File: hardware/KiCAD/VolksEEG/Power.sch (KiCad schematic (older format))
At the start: 27 parts, among them U3 LP3990MF-3.3, U4 LM2660MX, U5 TPS78425Q, U6 TPS72325Q

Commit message: Added Digi-key's kicad component libraries, some work done on power, think this will change but capturing it here for posterity.
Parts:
- removed C? (x2): 2.2u, Capacitor_SMD:C_0603_1608Metric_Pad1.08x0.95mm_HandSolder, symbol Device:C
- removed C?: 10u, Capacitor_SMD:C_0603_1608Metric_Pad1.08x0.95mm_HandSolder, symbol Device:C
- removed L?: 3.3u, symbol Device:L
- removed U3: LP3990MF-3.3, VolksEEG:SOT95P280X145-5N, symbol VolksEEG:LP3990MF-3.3
- added C? (x5): 100n, symbol Device:C
- added C? (x4): 1u, symbol Device:C
- added C?: 10u, Capacitor_SMD:C_0603_1608Metric_Pad1.08x0.95mm_HandSolder, symbol Device:C
- added C? (x2): 2.2u, Capacitor_SMD:C_0603_1608Metric_Pad1.08x0.95mm_HandSolder, symbol Device:C
- added C?: 10n, Capacitor_SMD:C_0603_1608Metric_Pad1.08x0.95mm_HandSolder, symbol Device:C
- added L?: 3.3u, symbol Device:L
- added U?: LP3990MF-3.3, VolksEEG:SOT95P280X145-5N, symbol VolksEEG:LP3990MF-3.3
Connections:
- net labels added: +2V5_ads, +3V3_ads, +5V_iso, -2V5_ads, GND2, VDD
- net labels removed: +3V3, GNDD, VDC
- wire segments 75 -> 130
- no-connect marks 5 -> 4
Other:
- note added: "3.3V Digital Voltage Supply"
- note removed: "3.3V Voltage Supply"
- moved on the sheet: C2, C4, C7, C8, C9, C?, L?, R?, U4, U5, U6

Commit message: Rejigged the power around so that the 3v3 supply is only generated once.
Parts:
- removed R?: 0, symbol Device:R
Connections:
- net labels added: +2V5_out, +3V3_out, -2V5_out
- net labels removed: +2V5_ads, +3V3_ads, -2V5_ads, GND2
- wire segments 130 -> 129
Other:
- moved on the sheet: C?
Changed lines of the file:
@@
 	2700 5300 3350 5300
 Wire Wire Line
-	2000 5300 1350 5300
+	2000 5300 1800 5300
 Wire Wire Line
 	1350 5300 1350 5150
@@
 Wire Wire Line
 	2000 4050 2000 3950
-Wire Wire Line
-	2000 5550 2000 5300
-Connection ~ 2000 5300
 Wire Wire Line
 	2000 5800 2000 5700
@@
 L power:GNDA #PWR?
 U 1 1 61837039
-P 4900 2300
-F 0 "#PWR?" H 4900 2050 50  0001 C CNN
-F 1 "GNDA" H 4905 2127 50  0000 C CNN
-F 2 "" H 4900 2300 50  0001 C CNN
-F 3 "" H 4900 2300 50  0001 C CNN
-	1    4900 2300
-	1    0    0    -1
-$EndComp
-$Comp
-L Device:R R?
-U 1 1 61837EDF
-P 3200 2200
-F 0 "R?" V 2993 2200 50  0000 C CNN
-F 1 "0" V 3084 2200 50  0000 C CNN
-F 2 "" V 3130 2200 50  0001 C CNN
-F 3 "~" H 3200 2200 50  0001 C CNN
-	1    3200 2200
-	0    1    1    0
+P 4900 1950
+F 0 "#PWR?" H 4900 1700 50  0001 C CNN
+F 1 "GNDA" H 4905 1777 50  0000 C CNN
+F 2 "" H 4900 1950 50  0001 C CNN
+F 3 "" H 4900 1950 50  0001 C CNN
+	1    4900 1950
+	1    0    0    -1
 $EndComp
 $Comp
@@
 L Device:C C?
 U 1 1 6195A2BF
-P 1500 1550
+P 1850 1550
 AR Path="/615BA255/6195A2BF" Ref="C?"  Part="1"
 AR Path="/61731DC5/6195A2BF" Ref="C?"  Part="1"
-F 0 "C?" H 1615 1596 50  0000 L CNN
-F 1 "2.2u" H 1615 1505 50  0000 L CNN
-F 2 "Capacitor_SMD:C_0603_1608Metric_Pad1.08x0.95mm_HandSolder" H 1538 1400 50  0001 C CNN
-F 3 "~" H 1500 1550 50  0001 C CNN
-	1    1500 1550
-	1    0    0    -1
-$EndComp
-Wire Wire Line
-	1500 1800 1500 1700
+F 0 "C?" H 1965 1596 50  0000 L CNN
+F 1 "2.2u" H 1965 1505 50  0000 L CNN
+F 2 "Capacitor_SMD:C_0603_1608Metric_Pad1.08x0.95mm_HandSolder" H 1888 1400 50  0001 C CNN
+F 3 "~" H 1850 1550 50  0001 C CNN
+	1    1850 1550
+	1    0    0    -1
+$EndComp
 Wire Wire Line
 	3800 1400 3800 1300
@@
 	1    0    0    -1
 $EndComp
-$Comp
-L power:GND2 #PWR?
-U 1 1 6195A2DE
-P 1500 1800
-AR Path="/61731DC5/6195A2DE" Ref="#PWR?"  Part="1"
-AR Path="/615BA255/6195A2DE" Ref="#PWR?"  Part="1"
-F 0 "#PWR?" H 1500 1550 50  0001 C CNN
-F 1 "GND2" H 1505 1627 50  0000 C CNN
-F 2 "" H 1500 1800 50  0001 C CNN
-F 3 "" H 1500 1800 50  0001 C CNN
-	1    1500 1800
-	1    0    0    -1
-$EndComp
-$Comp
-L power:GND2 #PWR?
-U 1 1 6195A2E4
-P 2450 2300
-AR Path="/61731DC5/6195A2E4" Ref="#PWR?"  Part="1"
-AR Path="/615BA255/6195A2E4" Ref="#PWR?"  Part="1"
-F 0 "#PWR?" H 2450 2050 50  0001 C CNN
-F 1 "GND2" H 2455 2127 50  0000 C CNN
-F 2 "" H 2450 2300 50  0001 C CNN
-F 3 "" H 2450 2300 50  0001 C CNN
-	1    2450 2300
-	1    0    0    -1
-$EndComp
-Wire Wire Line
-	1500 1400 1500 1300
-Connection ~ 1500 1300
-Wire Wire Line
-	2200 1550 2450 1550
-Text HLabel 1150 1300 0    50   Output ~ 0
+Wire Wire Line
+	1850 1400 1850 1300
+Text HLabel 1500 1300 0    50   Input ~ 0
 +5V_iso
 Wire Wire Line
-	1150 1300 1500 1300
+	1500 1300 1850 1300
 Wire Wire Line
 	4900 1150 4900 1300
@@
 	1    0    0    -1
 $EndComp
-Text HLabel 5100 1300 2    50   Input ~ 0
-+3V3_ads
+Text HLabel 5100 1300 2    50   Output ~ 0
++3V3_out
 Wire Wire Line
 	5100 1300 4900 1300
@@
 	1    0    0    -1
 $EndComp
-Wire Wire Line
-	2450 1700 2450 2200
-Connection ~ 2450 2200
-Wire Wire Line
-	2450 2200 2450 2300
 $Comp
 L power:GNDA #PWR?
 U 1 1 61970A4A
-P 3800 2300
-F 0 "#PWR?" H 3800 2050 50  0001 C CNN
-F 1 "GNDA" H 3805 2127 50  0000 C CNN
-F 2 "" H 3800 2300 50  0001 C CNN
-F 3 "" H 3800 2300 50  0001 C CNN
-	1    3800 2300
-	1    0    0    -1
-$EndComp
-Wire Wire Line
-	4900 1700 4900 2300
-Wire Wire Line
-	2450 2200 3050 2200
-Wire Wire Line
-	3800 1700 3800 2200
-Wire Wire Line
-	3350 2200 3800 2200
-Connection ~ 3800 2200
-Wire Wire Line
-	3800 2200 3800 2300
-Wire Wire Line
-	1500 1300 2200 1300
-Wire Wire Line
-	2200 1550 2200 1300
-Connection ~ 2200 1300
-Wire Wire Line
-	2200 1300 2450 1300
+P 3800 1950
+F 0 "#PWR?" H 3800 1700 50  0001 C CNN
+F 1 "GNDA" H 3805 1777 50  0000 C CNN
+F 2 "" H 3800 1950 50  0001 C CNN
+F 3 "" H 3800 1950 50  0001 C CNN
+	1    3800 1950
+	1    0    0    -1
+$EndComp
 Wire Wire Line
 	2000 3800 1850 3800
@@
 	1850 3550 2000 3550
 Text HLabel 5600 3550 2    50   Output ~ 0
-+2V5_ads
++2V5_out
 Text HLabel 5550 5300 2    50   Output ~ 0
--2V5_ads
+-2V5_out
 $Comp
 L Device:C C?
@@
 Wire Wire Line
 	5300 5300 5550 5300
+Wire Wire Line
+	2450 1550 2300 1550
+Wire Wire Line
+	2300 1550 2300 1300
+Wire Wire Line
+	2300 1300 2450 1300
+Wire Wire Line
+	1850 1300 2300 1300
+Connection ~ 1850 1300
+Connection ~ 2300 1300
+$Comp
+L power:GNDA #PWR?
+U 1 1 61A49E67
+P 2300 1950
+F 0 "#PWR?" H 2300 1700 50  0001 C CNN
+F 1 "GNDA" H 2305 1777 50  0000 C CNN
+F 2 "" H 2300 1950 50  0001 C CNN
+F 3 "" H 2300 1950 50  0001 C CNN
+	1    2300 1950
+	1    0    0    -1
+$EndComp
+$Comp
+L power:GNDA #PWR?
+U 1 1 61A4A061
+P 1850 1950
+F 0 "#PWR?" H 1850 1700 50  0001 C CNN
+F 1 "GNDA" H 1855 1777 50  0000 C CNN
+F 2 "" H 1850 1950 50  0001 C CNN
+F 3 "" H 1850 1950 50  0001 C CNN
+	1    1850 1950
+	1    0    0    -1
+$EndComp
+Wire Wire Line
+	1850 1700 1850 1950
+Wire Wire Line
+	2300 1950 2300 1700
+Wire Wire Line
+	2300 1700 2450 1700
+Wire Wire Line
+	3800 1950 3800 1700
+Wire Wire Line
+	4900 1700 4900 1950
+Wire Wire Line
+	2000 5550 1800 5550
+Wire Wire Line
+	1800 5550 1800 5300
+Connection ~ 1800 5300
+Wire Wire Line
+	1800 5300 1350 5300
 $EndSCHEMATC

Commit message: Updated names of heirarchical pins, finished referential montage configuration, added filter cap to ADS_nRST line, started putting ADS1299 gpios to a header.
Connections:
- net labels added: +2V5, +3V3, +5V, -2V5
- net labels removed: +2V5_out, +3V3_out, +5V_iso, -2V5_out
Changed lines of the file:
@@
 	1850 1400 1850 1300
 Text HLabel 1500 1300 0    50   Input ~ 0
-+5V_iso
++5V
 Wire Wire Line
 	1500 1300 1850 1300
@@
 $EndComp
 Text HLabel 5100 1300 2    50   Output ~ 0
-+3V3_out
++3V3
 Wire Wire Line
 	5100 1300 4900 1300
@@
 	1850 3550 2000 3550
 Text HLabel 5600 3550 2    50   Output ~ 0
-+2V5_out
++2V5
 Text HLabel 5550 5300 2    50   Output ~ 0
--2V5_out
+-2V5
 $Comp
 L Device:C C?

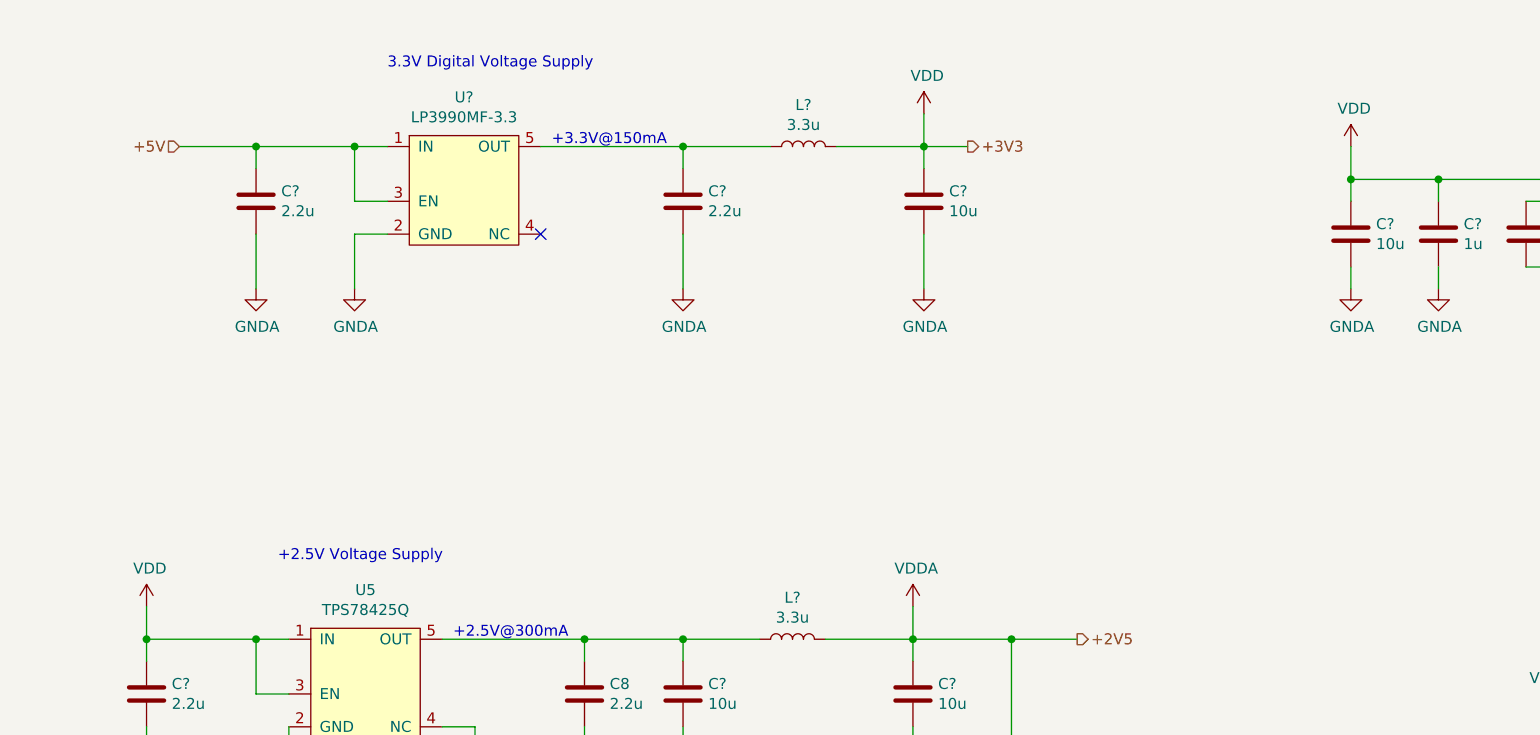
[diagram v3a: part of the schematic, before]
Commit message: Added custom power symbols for non isolated power. Seperated Analogue and digital supplies. finished putting the ADS1299 GPIOs to a header.
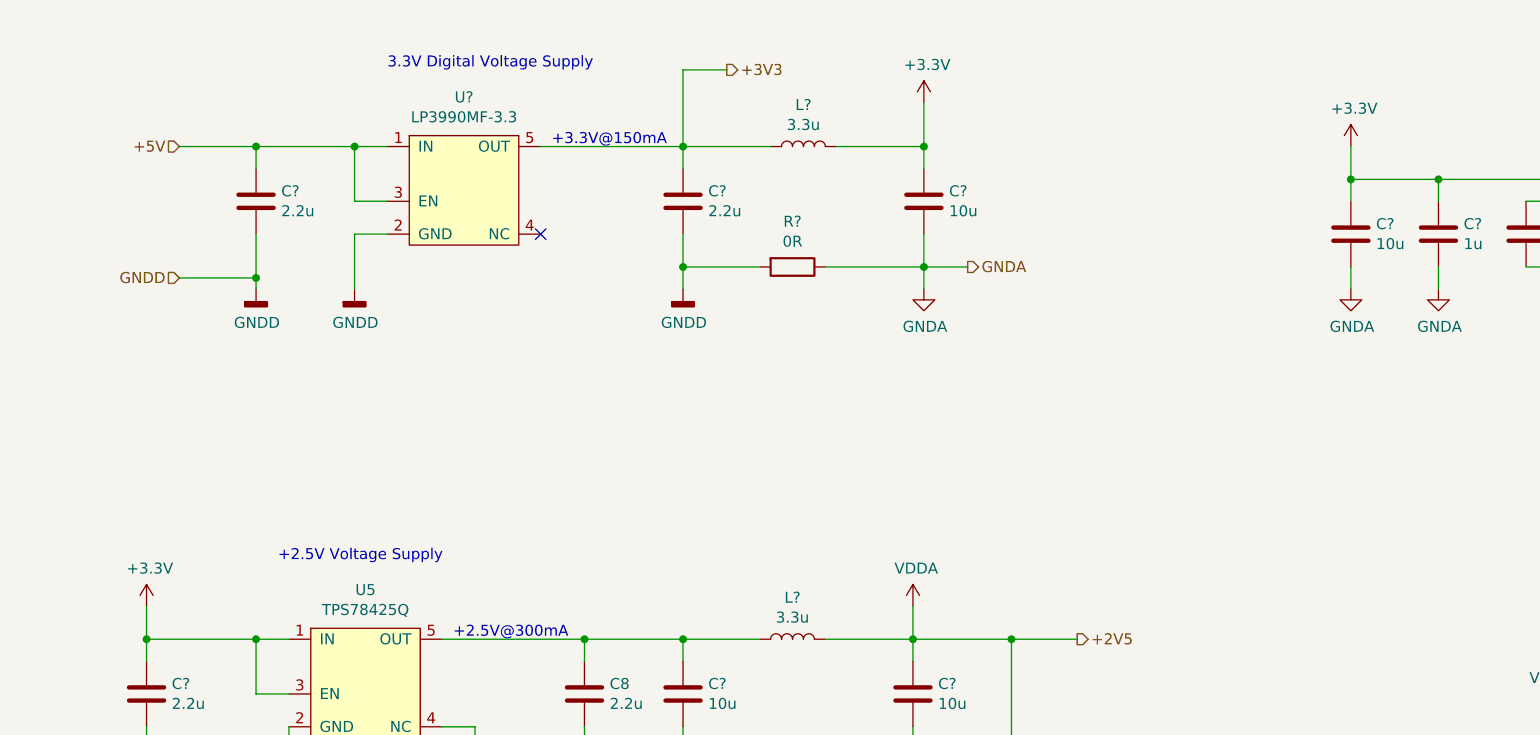
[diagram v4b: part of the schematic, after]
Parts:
- added R?: 0R, symbol Device:R
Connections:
- net labels added: +3.3V, GNDD
- wire segments 129 -> 137
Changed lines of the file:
@@
 	1500 1300 1850 1300
 Wire Wire Line
-	4900 1150 4900 1300
-$Comp
-L power:VDD #PWR?
-U 1 1 61963391
-P 4900 1150
-F 0 "#PWR?" H 4900 1000 50  0001 C CNN
-F 1 "VDD" H 4915 1323 50  0000 C CNN
-F 2 "" H 4900 1150 50  0001 C CNN
-F 3 "" H 4900 1150 50  0001 C CNN
-	1    4900 1150
-	1    0    0    -1
-$EndComp
-Text HLabel 5100 1300 2    50   Output ~ 0
+	4900 1100 4900 1300
+Text HLabel 4000 950  2    50   Output ~ 0
 +3V3
-Wire Wire Line
-	5100 1300 4900 1300
-$Comp
-L power:VDD #PWR?
-U 1 1 6196789C
-P 6850 1300
-F 0 "#PWR?" H 6850 1150 50  0001 C CNN
-F 1 "VDD" H 6865 1473 50  0000 C CNN
-F 2 "" H 6850 1300 50  0001 C CNN
-F 3 "" H 6850 1300 50  0001 C CNN
-	1    6850 1300
-	1    0    0    -1
-$EndComp
-$Comp
-L power:VDD #PWR?
-U 1 1 619682BB
-P 1350 3400
-F 0 "#PWR?" H 1350 3250 50  0001 C CNN
-F 1 "VDD" H 1365 3573 50  0000 C CNN
-F 2 "" H 1350 3400 50  0001 C CNN
-F 3 "" H 1350 3400 50  0001 C CNN
-	1    1350 3400
-	1    0    0    -1
-$EndComp
-$Comp
-L power:GNDA #PWR?
-U 1 1 61970A4A
-P 3800 1950
-F 0 "#PWR?" H 3800 1700 50  0001 C CNN
-F 1 "GNDA" H 3805 1777 50  0000 C CNN
-F 2 "" H 3800 1950 50  0001 C CNN
-F 3 "" H 3800 1950 50  0001 C CNN
-	1    3800 1950
-	1    0    0    -1
-$EndComp
 Wire Wire Line
 	2000 3800 1850 3800
@@
 Connection ~ 1850 1300
 Connection ~ 2300 1300
-$Comp
-L power:GNDA #PWR?
-U 1 1 61A49E67
+Wire Wire Line
+	1850 1700 1850 1900
+Wire Wire Line
+	2300 1950 2300 1700
+Wire Wire Line
+	2300 1700 2450 1700
+Wire Wire Line
+	3800 1950 3800 1850
+Wire Wire Line
+	2000 5550 1800 5550
+Wire Wire Line
+	1800 5550 1800 5300
+Connection ~ 1800 5300
+Wire Wire Line
+	1800 5300 1350 5300
+$Comp
+L Device:R R?
+U 1 1 61C452C6
+P 4300 1850
+F 0 "R?" V 4093 1850 50  0000 C CNN
+F 1 "0R" V 4184 1850 50  0000 C CNN
+F 2 "" V 4230 1850 50  0001 C CNN
+F 3 "~" H 4300 1850 50  0001 C CNN
+	1    4300 1850
+	0    1    1    0
+$EndComp
+Wire Wire Line
+	4150 1850 3800 1850
+Connection ~ 3800 1850
+Wire Wire Line
+	3800 1850 3800 1700
+Wire Wire Line
+	4450 1850 4900 1850
+Wire Wire Line
+	4900 1700 4900 1850
+Connection ~ 4900 1850
+Wire Wire Line
+	4900 1850 4900 1950
+Text HLabel 1500 1900 0    50   Input ~ 0
+GNDD
+Wire Wire Line
+	1500 1900 1850 1900
+Connection ~ 1850 1900
+Wire Wire Line
+	1850 1900 1850 1950
+Text HLabel 5100 1850 2    50   Output ~ 0
+GNDA
+Wire Wire Line
+	4900 1850 5100 1850
+$Comp
+L power:GNDD #PWR?
+U 1 1 61C5E767
+P 1850 1950
+AR Path="/615BA20B/61C5E767" Ref="#PWR?"  Part="1"
+AR Path="/61731DC5/61C5E767" Ref="#PWR?"  Part="1"
+AR Path="/615BA255/61C5E767" Ref="#PWR?"  Part="1"
+F 0 "#PWR?" H 1850 1700 50  0001 C CNN
+F 1 "GNDD" H 1854 1795 50  0000 C CNN
+F 2 "" H 1850 1950 50  0001 C CNN
+F 3 "" H 1850 1950 50  0001 C CNN
+	1    1850 1950
+	1    0    0    -1
+$EndComp
+$Comp
+L power:GNDD #PWR?
+U 1 1 61C6348B
 P 2300 1950
+AR Path="/615BA20B/61C6348B" Ref="#PWR?"  Part="1"
+AR Path="/61731DC5/61C6348B" Ref="#PWR?"  Part="1"
+AR Path="/615BA255/61C6348B" Ref="#PWR?"  Part="1"
 F 0 "#PWR?" H 2300 1700 50  0001 C CNN
-F 1 "GNDA" H 2305 1777 50  0000 C CNN
+F 1 "GNDD" H 2304 1795 50  0000 C CNN
 F 2 "" H 2300 1950 50  0001 C CNN
 F 3 "" H 2300 1950 50  0001 C CNN
@@
 $EndComp
 $Comp
-L power:GNDA #PWR?
-U 1 1 61A4A061
-P 1850 1950
-F 0 "#PWR?" H 1850 1700 50  0001 C CNN
-F 1 "GNDA" H 1855 1777 50  0000 C CNN
-F 2 "" H 1850 1950 50  0001 C CNN
-F 3 "" H 1850 1950 50  0001 C CNN
-	1    1850 1950
-	1    0    0    -1
-$EndComp
-Wire Wire Line
-	1850 1700 1850 1950
-Wire Wire Line
-	2300 1950 2300 1700
-Wire Wire Line
-	2300 1700 2450 1700
-Wire Wire Line
-	3800 1950 3800 1700
-Wire Wire Line
-	4900 1700 4900 1950
-Wire Wire Line
-	2000 5550 1800 5550
-Wire Wire Line
-	1800 5550 1800 5300
-Connection ~ 1800 5300
-Wire Wire Line
-	1800 5300 1350 5300
+L power:GNDD #PWR?
+U 1 1 61C6367A
+P 3800 1950
+AR Path="/615BA20B/61C6367A" Ref="#PWR?"  Part="1"
+AR Path="/61731DC5/61C6367A" Ref="#PWR?"  Part="1"
+AR Path="/615BA255/61C6367A" Ref="#PWR?"  Part="1"
+F 0 "#PWR?" H 3800 1700 50  0001 C CNN
+F 1 "GNDD" H 3804 1795 50  0000 C CNN
+F 2 "" H 3800 1950 50  0001 C CNN
+F 3 "" H 3800 1950 50  0001 C CNN
+	1    3800 1950
+	1    0    0    -1
+$EndComp
+Wire Wire Line
+	3800 1300 3800 950
+Wire Wire Line
+	3800 950  4000 950
+$Comp
+L power:+3.3V #PWR?
+U 1 1 61C77BAD
+P 4900 1100
+F 0 "#PWR?" H 4900 950 50  0001 C CNN
+F 1 "+3.3V" H 4915 1273 50  0000 C CNN
+F 2 "" H 4900 1100 50  0001 C CNN
+F 3 "" H 4900 1100 50  0001 C CNN
+	1    4900 1100
+	1    0    0    -1
+$EndComp
+$Comp
+L power:+3.3V #PWR?
+U 1 1 61C7815B
+P 6850 1300
+F 0 "#PWR?" H 6850 1150 50  0001 C CNN
+F 1 "+3.3V" H 6865 1473 50  0000 C CNN
+F 2 "" H 6850 1300 50  0001 C CNN
+F 3 "" H 6850 1300 50  0001 C CNN
+	1    6850 1300
+	1    0    0    -1
+$EndComp
+$Comp
+L power:+3.3V #PWR?
+U 1 1 61C786AF
+P 1350 3400
+F 0 "#PWR?" H 1350 3250 50  0001 C CNN
+F 1 "+3.3V" H 1365 3573 50  0000 C CNN
+F 2 "" H 1350 3400 50  0001 C CNN
+F 3 "" H 1350 3400 50  0001 C CNN
+	1    1350 3400
+	1    0    0    -1
+$EndComp
 $EndSCHEMATC

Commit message: Tweaks based on feedback, Changed digital isolators to ADUM240E devices due to component availability.
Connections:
- net labels added: +3V3A, -3V3A
- net labels removed: +3.3V, -3V3
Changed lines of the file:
@@
 $Descr A4 11693 8268
 encoding utf-8
-Sheet 3 6
+Sheet 5 6
 Title ""
 Date ""
@@
 F 3 "" H 4850 5150 50  0001 C CNN
 	1    4850 5150
-	1    0    0    -1
-$EndComp
-$Comp
-L power:-3V3 #PWR018
-U 1 1 61617464
-P 1350 5150
-F 0 "#PWR018" H 1350 5250 50  0001 C CNN
-F 1 "-3V3" H 1365 5323 50  0000 C CNN
-F 2 "" H 1350 5150 50  0001 C CNN
-F 3 "" H 1350 5150 50  0001 C CNN
-	1    1350 5150
 	1    0    0    -1
 $EndComp
@@
 F 5 "https://eu.mouser.com/ProductDetail/Texas-Instruments/LM2660MX-NOPB?qs=%2Fha2pyFadugHGOygNHaYnDjgJHODW6F6O01kwvJjsKBnt2qN9JbSfA%3D%3D" H 8350 1650 50  0001 C CNN "Supplier 2 Link"
 	1    8350 1650
-	1    0    0    -1
-$EndComp
-$Comp
-L power:-3V3 #PWR014
-U 1 1 61614616
-P 10500 1300
-F 0 "#PWR014" H 10500 1400 50  0001 C CNN
-F 1 "-3V3" H 10515 1473 50  0000 C CNN
-F 2 "" H 10500 1300 50  0001 C CNN
-F 3 "" H 10500 1300 50  0001 C CNN
-	1    10500 1300
 	1    0    0    -1
 $EndComp
@@
 	3800 950  4000 950
 $Comp
-L power:+3.3V #PWR?
-U 1 1 61C77BAD
+L VolksEEG:+3V3A #PWR?
+U 1 1 61CE45B3
 P 4900 1100
 F 0 "#PWR?" H 4900 950 50  0001 C CNN
-F 1 "+3.3V" H 4915 1273 50  0000 C CNN
+F 1 "+3V3A" H 4915 1273 50  0000 C CNN
 F 2 "" H 4900 1100 50  0001 C CNN
 F 3 "" H 4900 1100 50  0001 C CNN
@@
 $EndComp
 $Comp
-L power:+3.3V #PWR?
-U 1 1 61C7815B
+L VolksEEG:+3V3A #PWR?
+U 1 1 61CE4ACE
 P 6850 1300
 F 0 "#PWR?" H 6850 1150 50  0001 C CNN
-F 1 "+3.3V" H 6865 1473 50  0000 C CNN
+F 1 "+3V3A" H 6865 1473 50  0000 C CNN
 F 2 "" H 6850 1300 50  0001 C CNN
 F 3 "" H 6850 1300 50  0001 C CNN
@@
 $EndComp
 $Comp
-L power:+3.3V #PWR?
-U 1 1 61C786AF
+L VolksEEG:+3V3A #PWR?
+U 1 1 61CE56F9
 P 1350 3400
 F 0 "#PWR?" H 1350 3250 50  0001 C CNN
-F 1 "+3.3V" H 1365 3573 50  0000 C CNN
+F 1 "+3V3A" H 1365 3573 50  0000 C CNN
 F 2 "" H 1350 3400 50  0001 C CNN
 F 3 "" H 1350 3400 50  0001 C CNN
@@
 	1    0    0    -1
 $EndComp
+$Comp
+L VolksEEG:-3V3A #PWR?
+U 1 1 61CE6601
+P 10500 1300
+F 0 "#PWR?" H 10500 1150 50  0001 C CNN
+F 1 "-3V3A" H 10515 1473 50  0000 C CNN
+F 2 "" H 10500 1300 50  0001 C CNN
+F 3 "" H 10500 1300 50  0001 C CNN
+	1    10500 1300
+	1    0    0    -1
+$EndComp
+$Comp
+L VolksEEG:-3V3A #PWR?
+U 1 1 61CE6D2F
+P 1350 5150
+F 0 "#PWR?" H 1350 5000 50  0001 C CNN
+F 1 "-3V3A" H 1365 5323 50  0000 C CNN
+F 2 "" H 1350 5150 50  0001 C CNN
+F 3 "" H 1350 5150 50  0001 C CNN
+	1    1350 5150
+	1    0    0    -1
+$EndComp
